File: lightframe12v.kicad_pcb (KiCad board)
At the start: 2 copper layers, 91.4 x 45.7 mm, 52 parts, among them J1 PJ-077, J2 Conn_01x08_Female, J3 Conn_01x08_Female, J4 Conn_01x06_Female, Q1 MMBT2222, Q2 MMBT2222, SW1 SW_Push, SW2 SW_Push, U1 TPS563207s, U2 TLC6C598PWR, U3 ESP32-WROOM-32U, U4 TLC6C598PWR

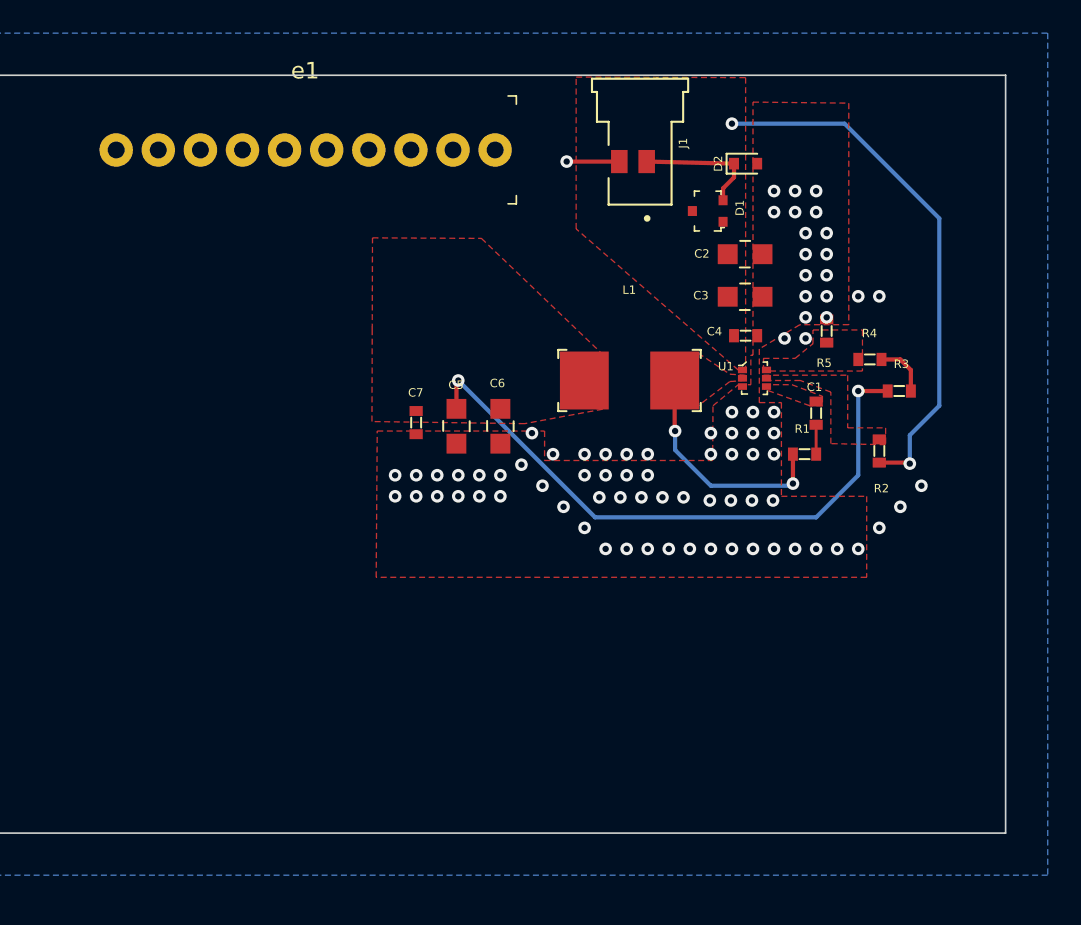
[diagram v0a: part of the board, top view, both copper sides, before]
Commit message: Adds fiducials.
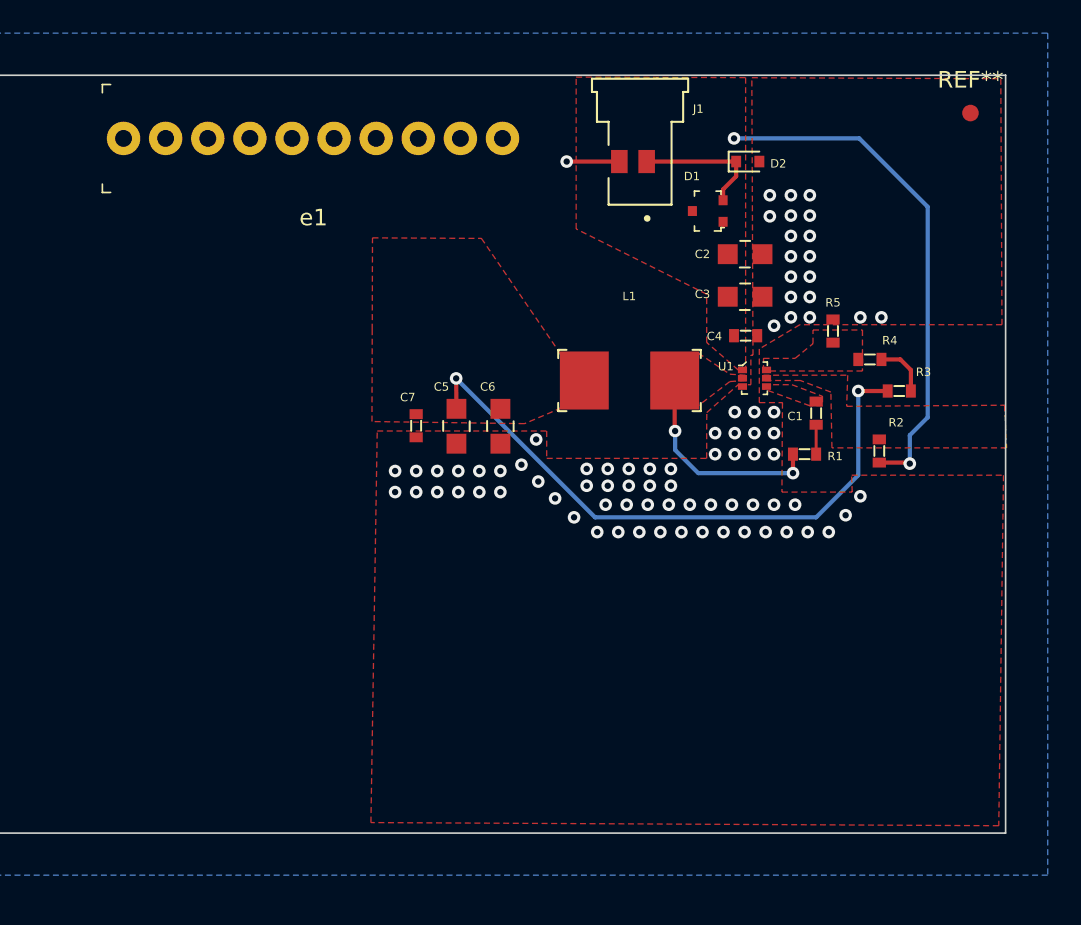
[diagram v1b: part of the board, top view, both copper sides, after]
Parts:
- added REF**: Fiducial_1mm_Mask2mm, Fiducial:Fiducial_1mm_Mask2mm, F.Cu at (361.1, -536.2)
- R4: value 3.09k -> 30.9k
- moved e1 0.83 mm to (321.4, -534.7), turned to 0 degrees
- moved R5 0.38 mm to (352.8, -523.0)
- moved C7 0.19 mm to (327.7, -517.3)
- moved D2 0.18 mm to (347.7, -533.3)
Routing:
- net Net-(L1-Pad1): track 14.5 -> 13.2 mm
- net +12V: track 32.2 -> 31.2 mm
- net (no net): vias 1 -> 0

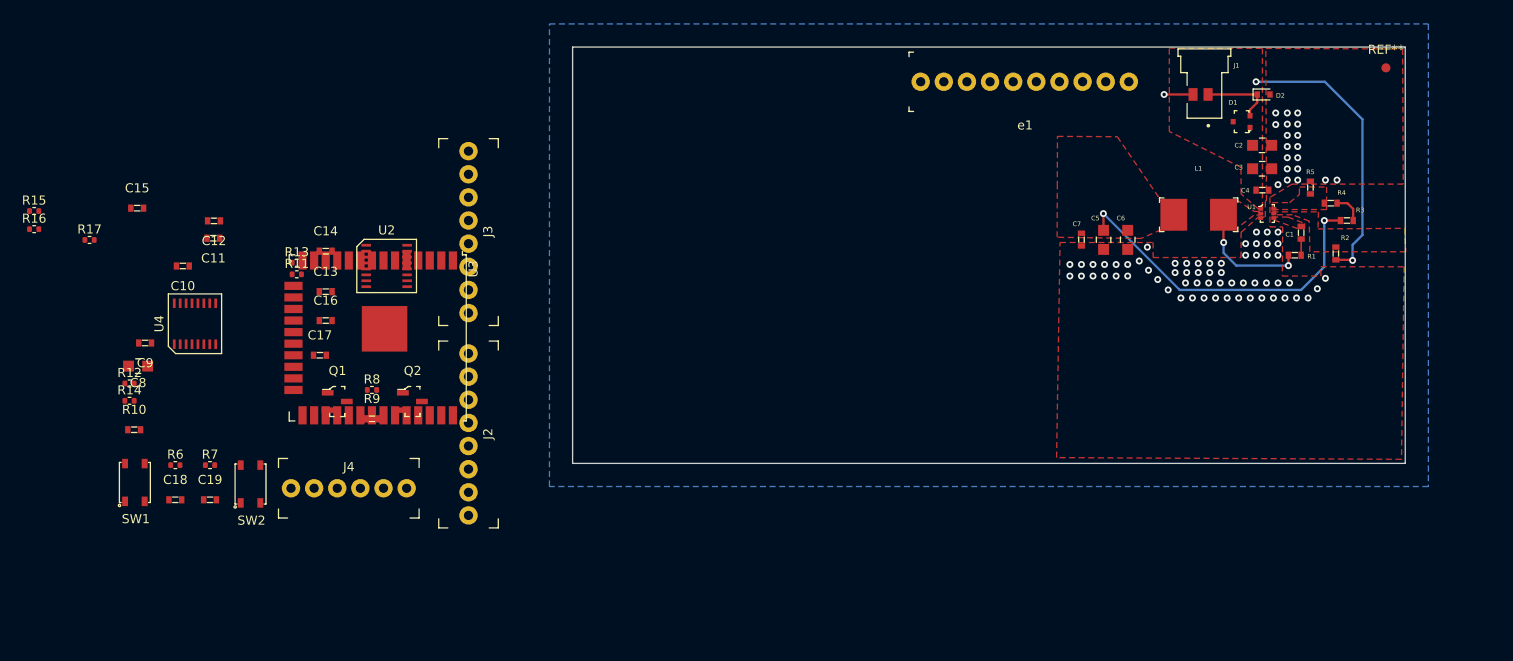
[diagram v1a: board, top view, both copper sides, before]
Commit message: Updates header footprints.
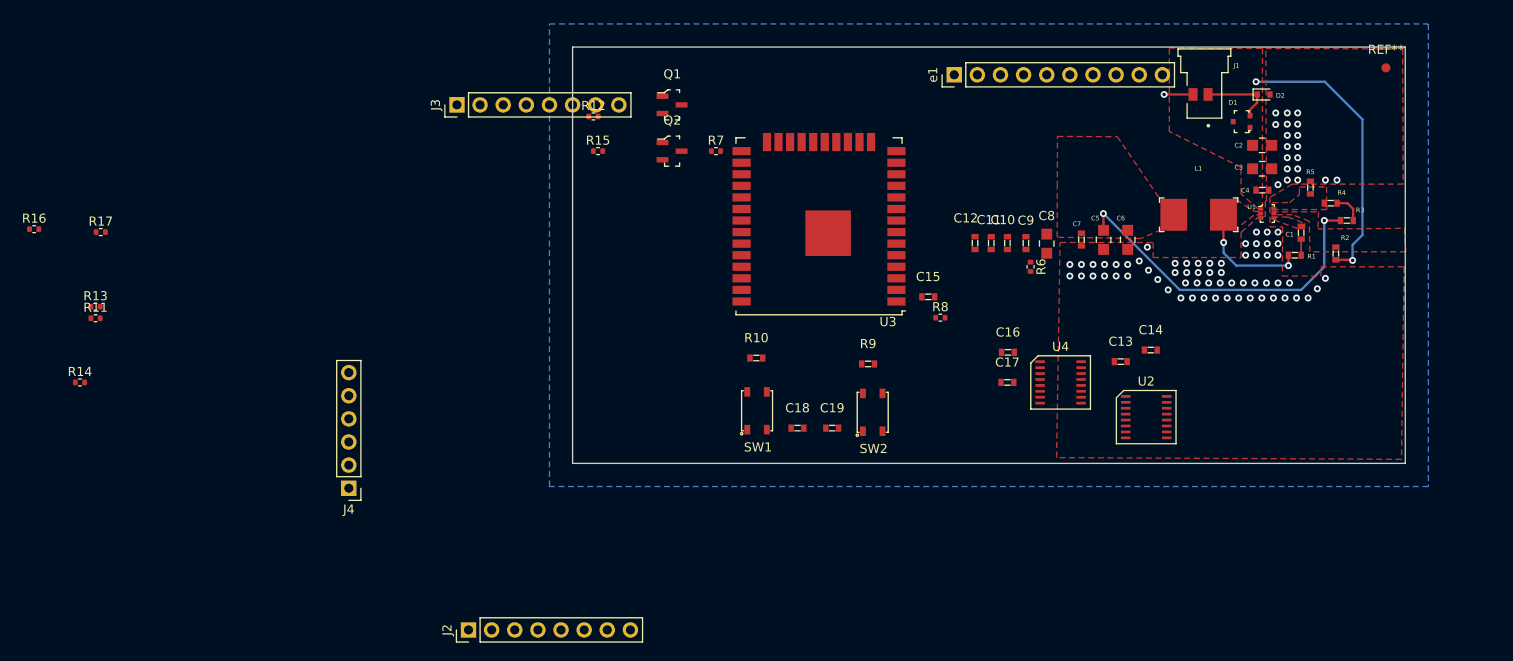
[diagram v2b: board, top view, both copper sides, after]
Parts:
- J2, J3: footprint keith:Pinheader1x8 2.54_Drill1.02mm -> Connector_PinHeader_2.54mm:PinHeader_1x08_P2.54mm_Vertical
- J4: footprint keith:Pinheader1x6 2.54_Drill1.02mm -> Connector_PinHeader_2.54mm:PinHeader_1x06_P2.54mm_Vertical
- e1: footprint keith:Pinheader1x10 2.54_Drill1.02mm -> Connector_PinHeader_2.54mm:PinHeader_1x10_P2.54mm_Vertical
- moved C8 100.7 mm to (323.9, -516.9), turned to 270 degrees
- moved C9 97.3 mm to (321.6, -517.0), turned to 270 degrees
- moved R6 96.4 mm to (322.1, -514.4), turned to 270 degrees
- moved U4 95.3 mm to (325.4, -501.6), turned to 270 degrees
- moved C14 91.3 mm to (335.3, -505.2)
- moved C10 90.6 mm to (319.5, -517.0), turned to 270 degrees
- moved C13 87.6 mm to (332.0, -503.9)
- moved C15 87.4 mm to (310.8, -511.0)
- moved C11 85.4 mm to (317.8, -517.0), turned to 270 degrees
- moved U2 85.0 mm to (334.8, -497.8)
- moved C12 83.6 mm to (316.0, -517.0), turned to 270 degrees
- moved C17 75.6 mm to (319.5, -501.6)
- moved C16 75.0 mm to (319.6, -505.0)
- moved R10 68.8 mm to (292.0, -504.3)
- moved C18 68.8 mm to (296.5, -496.6)
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
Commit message: creates new symbol TLC5971
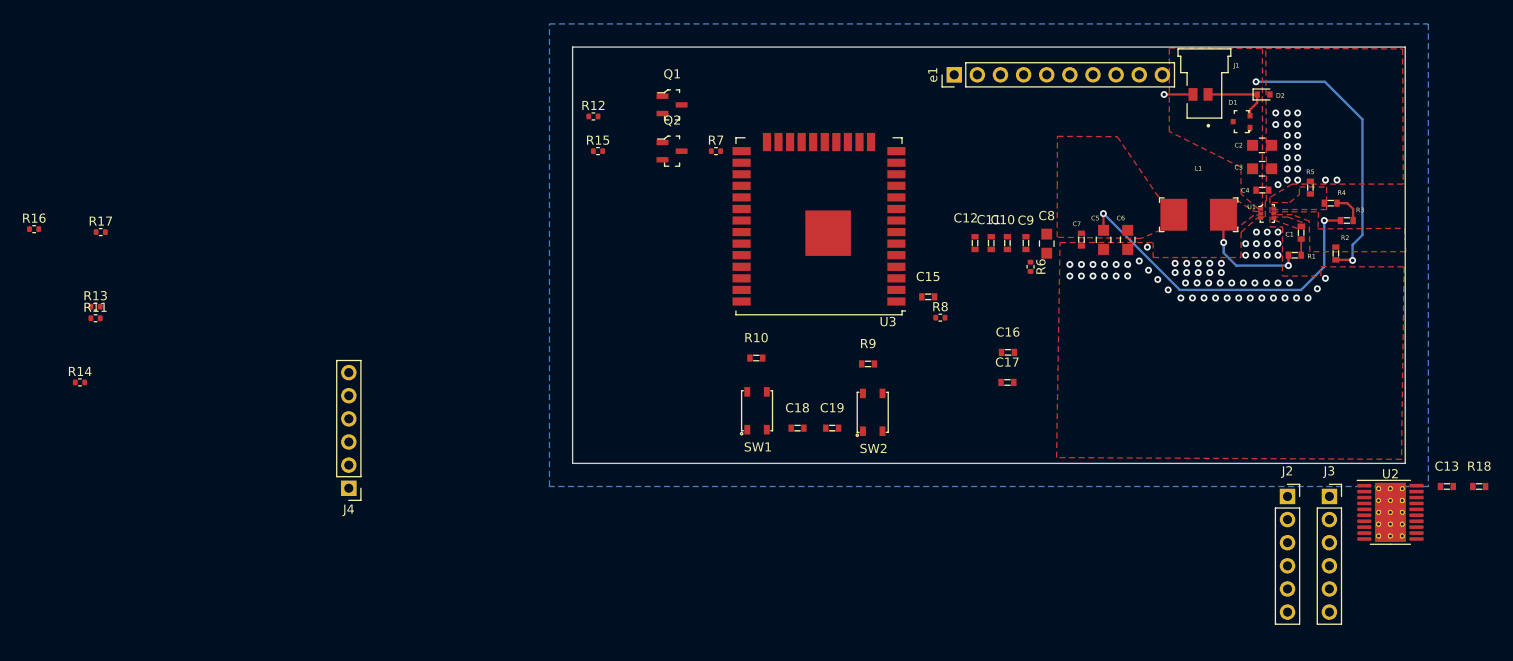
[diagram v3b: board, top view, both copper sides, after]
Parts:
- removed C14: 0.1uF, digikey-footprints:0603
- removed REF**: Fiducial_1mm_Mask2mm, Fiducial:Fiducial_1mm_Mask2mm
- removed U4: TLC6C598PWR, keith:TLC6C598
- added R18: 820, digikey-footprints:0603, F.Cu at (371.3, -490.2)
- J2, J3: value Conn_01x08_Female -> Conn_01x06_Female; footprint Connector_PinHeader_2.54mm:PinHeader_1x08_P2.54mm_Vertical -> Connector_PinSocket_2.54mm:PinSocket_1x06_P2.54mm_Vertical
- U2: value TLC6C598PWR -> TLC5971; footprint keith:TLC6C598 -> Package_SO:HTSSOP-20-1EP_4.4x6.5mm_P0.65mm_EP3.4x6.5mm_Mask2.75x3.43mm_ThermalVias
- moved J3 105.0 mm to (354.9, -489.1), turned to 0 degrees
- moved J2 91.1 mm to (350.3, -489.1), turned to 0 degrees
- moved C13 38.4 mm to (367.8, -490.2)
- moved U2 28.8 mm to (361.6, -487.4), turned to 0 degrees
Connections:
- C13 pad 1: +3V3 -> Net-(C13-Pad1)
- J2 pad 1: /Drain1 -> /LED1
- J2 pad 2: /Drain2 -> /LED2
- J2 pad 3: /Drain3 -> /LED3
- J2 pad 4: /Drain4 -> /LED4
- J2 pad 5: /Drain5 -> /LED5
- J2 pad 6: /Drain6 -> /LED6
- J3 pad 1: /Drain9 -> /LED7
- J3 pad 2: /Drain10 -> /LED8
- J3 pad 3: /Drain11 -> /LED9
- J3 pad 4: /Drain12 -> /LED10
- J3 pad 5: /Drain13 -> /LED11
- J3 pad 6: /Drain14 -> /LED12
- U2 pad 1: +3V3 -> Net-(R18-Pad1)
- U2 pad 10: /Register_Clock -> /Serial_Clock
- U2 pad 11: /Drain13 -> Net-(U2-Pad11)
- U2 pad 12: /Drain14 -> Net-(U2-Pad12)
- U2 pad 13: /Drain15 -> /LED7
- U2 pad 14: /Drain16 -> /LED8
- U2 pad 15: /Serial_Clock -> /LED9
- U2 pad 16: GND -> /LED10
- U2 pad 2: /Driver2_Serial_In -> GND
- U2 pad 3: /Drain9 -> /LED1
- U2 pad 4: /Drain10 -> /LED2
- U2 pad 5: /Drain11 -> /LED3
- U2 pad 6: /Drain12 -> /LED4
- U2 pad 7: /Clear -> /LED5
- U2 pad 8: /Enable -> /LED6
- U2 pad 9: Net-(U2-Pad9) -> /Serial_In

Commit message: initial layout of wroom
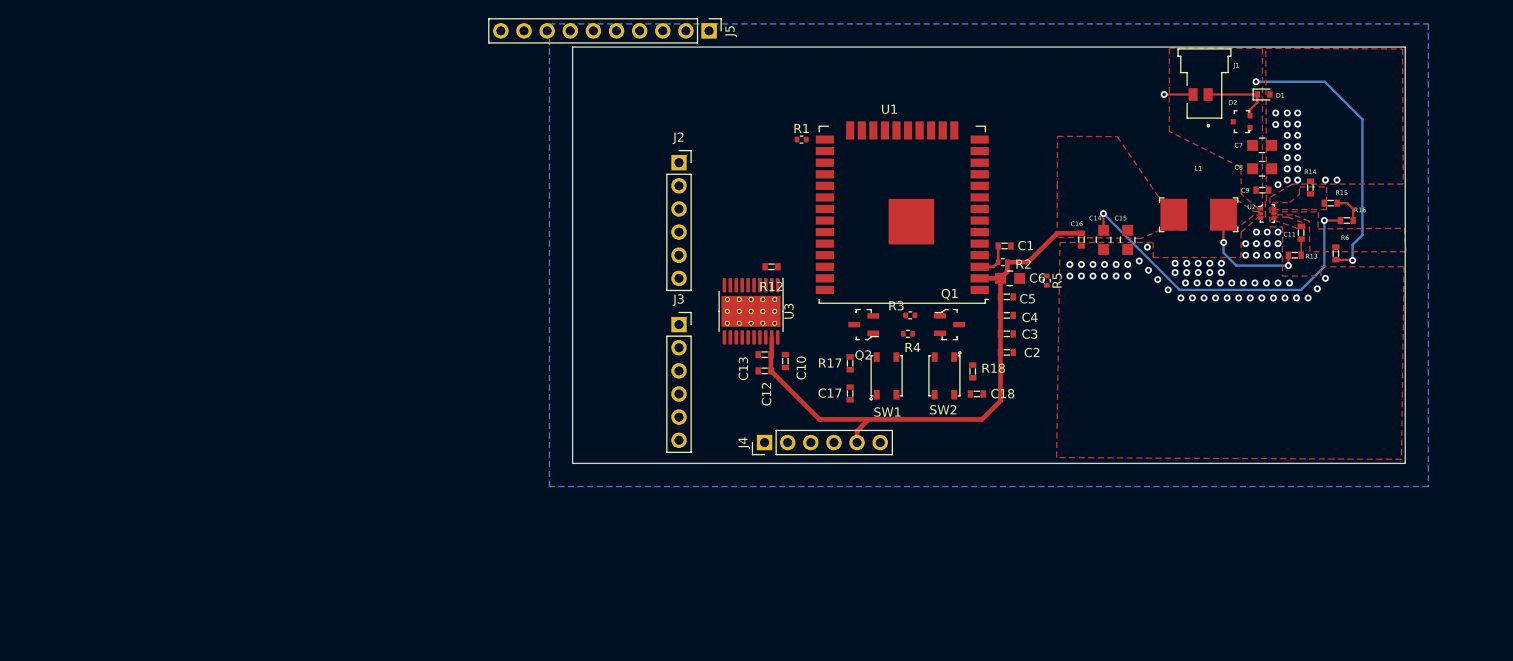
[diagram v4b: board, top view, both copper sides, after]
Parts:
- removed R11: 50 Ohms, Resistor_SMD:R_0402_1005Metric
- removed the R13 at (219.4, -510.0)
- removed the R14 at (217.7, -501.6)
- removed the R16 at (212.6, -518.5)
- removed the R17 at (220.0, -518.2)
- moved R12 81.4 mm to (293.6, -514.4), turned to 180 degrees
- moved J2 76.2 mm to (283.5, -525.8)
- moved C10 73.9 mm to (295.1, -504.0), turned to 270 degrees
- moved J3 73.9 mm to (283.5, -508.0)
- moved U3 73.6 mm to (291.4, -509.5), turned to 270 degrees
- moved J4 45.9 mm to (292.9, -495.0), turned to 90 degrees
- moved R3 41.1 mm to (308.9, -509.0), turned to 180 degrees
- moved R4 39.5 mm to (308.6, -507.0)
- moved Q1 38.9 mm to (313.2, -508.0)
- moved Q2 28.4 mm to (303.8, -508.0), turned to 180 degrees
- moved J5 27.4 mm to (286.8, -540.3), turned to 270 degrees
- moved C13 26.8 mm to (292.9, -504.7), turned to 180 degrees
- moved C12 26.8 mm to (292.9, -502.9), turned to 180 degrees
- moved R18 23.8 mm to (315.7, -502.9), turned to 90 degrees
- moved C18 16.3 mm to (316.2, -500.4), turned to 180 degrees
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- renumbered C15 to C1, C13 to C10, C1 to C11, C16 to C12, C17 to C13, C5 to C14, C6 to C15, C7 to C16, C18 to C17, C19 to C18, C11 to C2, C12 to C3, C10 to C4, C9 to C5, C8 to C6, C2 to C7, C3 to C8, C4 to C9, D2 to D1, D1 to D2, e1 to J5, R7 to R1, R18 to R12, R1 to R13, R5 to R14, R4 to R15, R3 to R16, R9 to R17, R10 to R18, R8 to R2, R12 to R3, R15 to R4, R6 to R5, R2 to R6, U3 to U1, U1 to U2, U2 to U3
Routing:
- net +3V3: track 38.4 -> 100.7 mm
- net /Reset: track 0.00 -> 4.02 mm

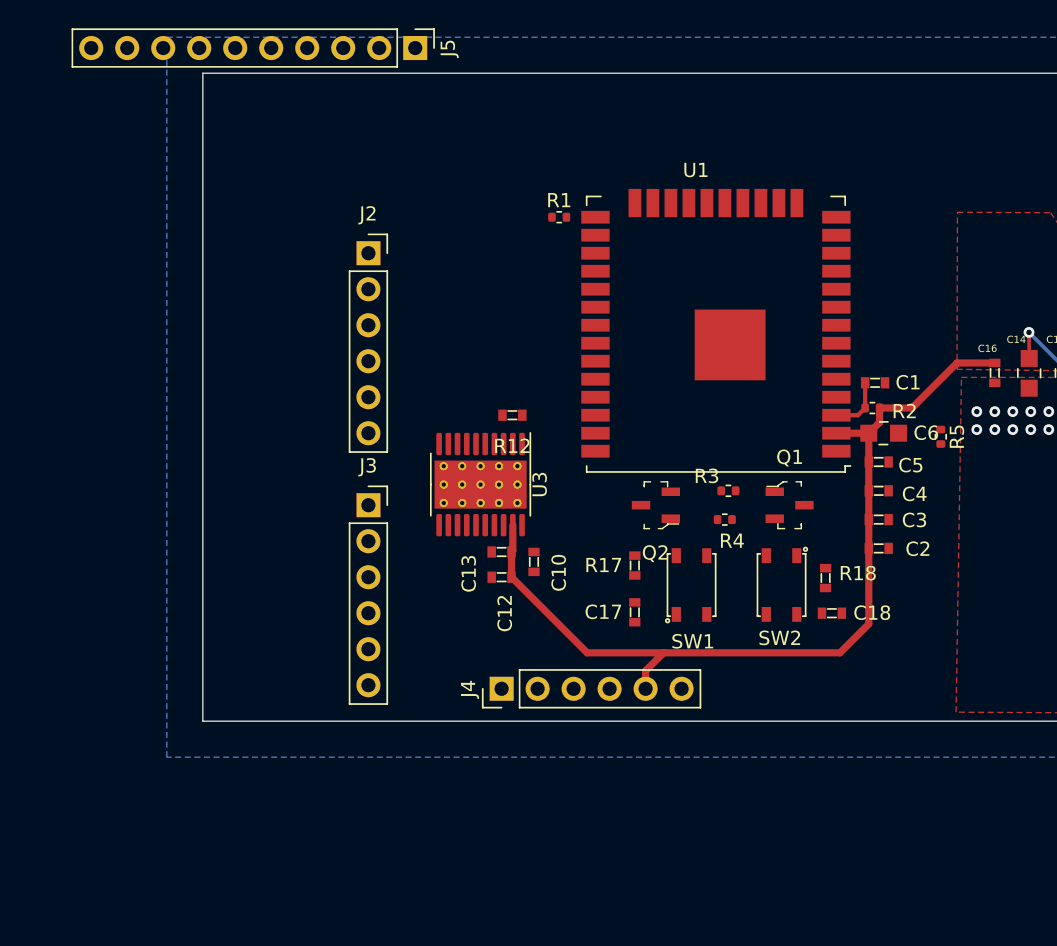
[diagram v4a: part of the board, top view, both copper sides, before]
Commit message: improves wroom layout
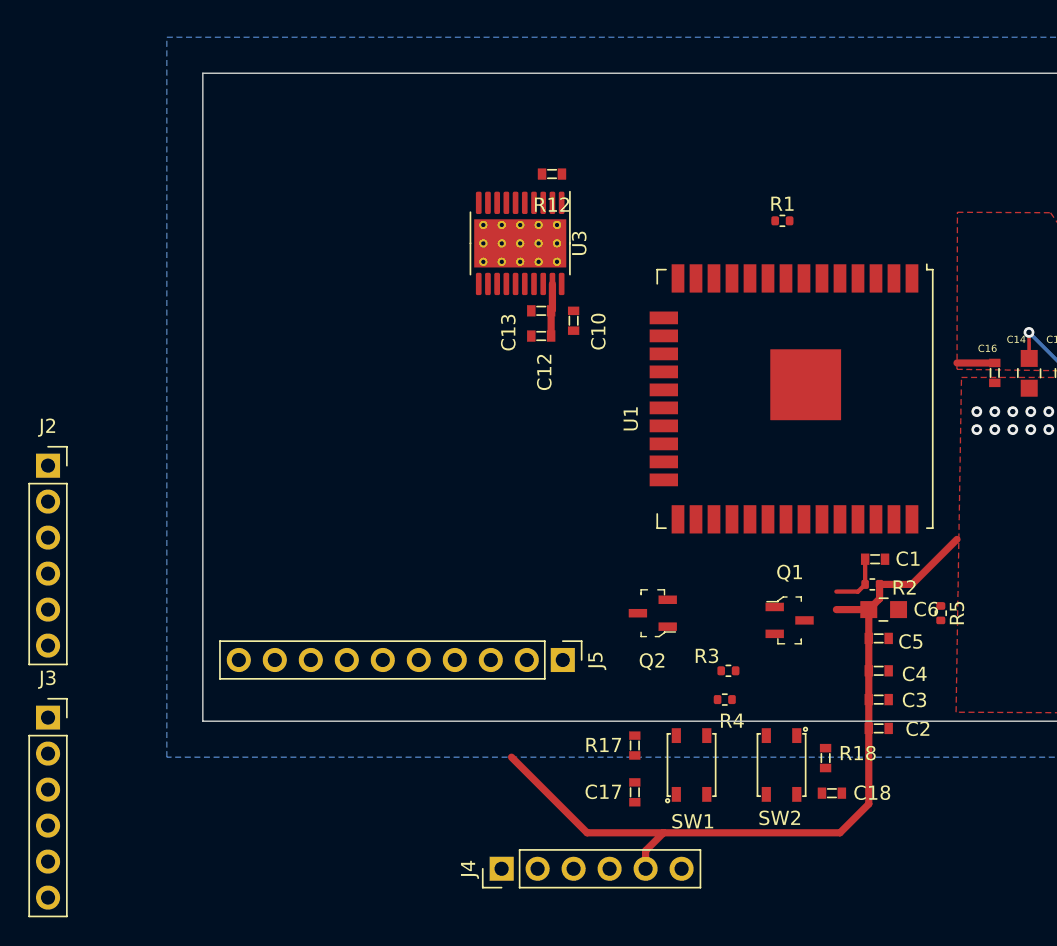
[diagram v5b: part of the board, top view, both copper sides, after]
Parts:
- moved J5 44.4 mm to (297.2, -497.1)
- moved J2 27.1 mm to (260.9, -510.8)
- moved J3 27.1 mm to (260.9, -493.0)
- moved C13 17.2 mm to (295.7, -521.7)
- moved R12 17.2 mm to (296.4, -531.4)
- moved C10 17.2 mm to (297.9, -521.0)
- moved C12 17.2 mm to (295.7, -519.9)
- moved U3 17.2 mm to (294.2, -526.5)
- moved R1 15.8 mm to (312.7, -528.1)
- moved C4 12.7 mm to (319.5, -496.3)
- moved R17 12.7 mm to (302.3, -491.0)
- moved R3 12.7 mm to (308.9, -496.3)
- moved SW1 12.7 mm to (306.3, -489.7)
- moved SW2 12.7 mm to (312.6, -489.7)
- moved C17 12.7 mm to (302.3, -487.7)
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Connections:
- net /Clear renamed Net-(U1-Pad10)
- net /Enable renamed Net-(U1-Pad11)
- net /Register_Clock renamed Net-(U1-Pad12)
- J5 pad 2: /Gpio14 -> Net-(J5-Pad2)
- J5 pad 4: /Gpio16 -> /Gpio22
- J5 pad 5: /Gpio17 -> /Gpio23
- U1 pad 13: /Gpio14 -> Net-(U1-Pad13)
- U1 pad 16: /Gpio13 -> /Serial_In
- U1 pad 23: /Gpio15 -> /Serial_Clock
- U1 pad 27: /Gpio16 -> /Gpio13
- U1 pad 28: /Gpio17 -> /Gpio15
- U1 pad 36: /Serial_In -> /Gpio22
- U1 pad 37: /Serial_Clock -> /Gpio23
